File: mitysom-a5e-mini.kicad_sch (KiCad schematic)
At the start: 1 part, among them J1 Plug_Samtec_SEAM-50-02.0-L-08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

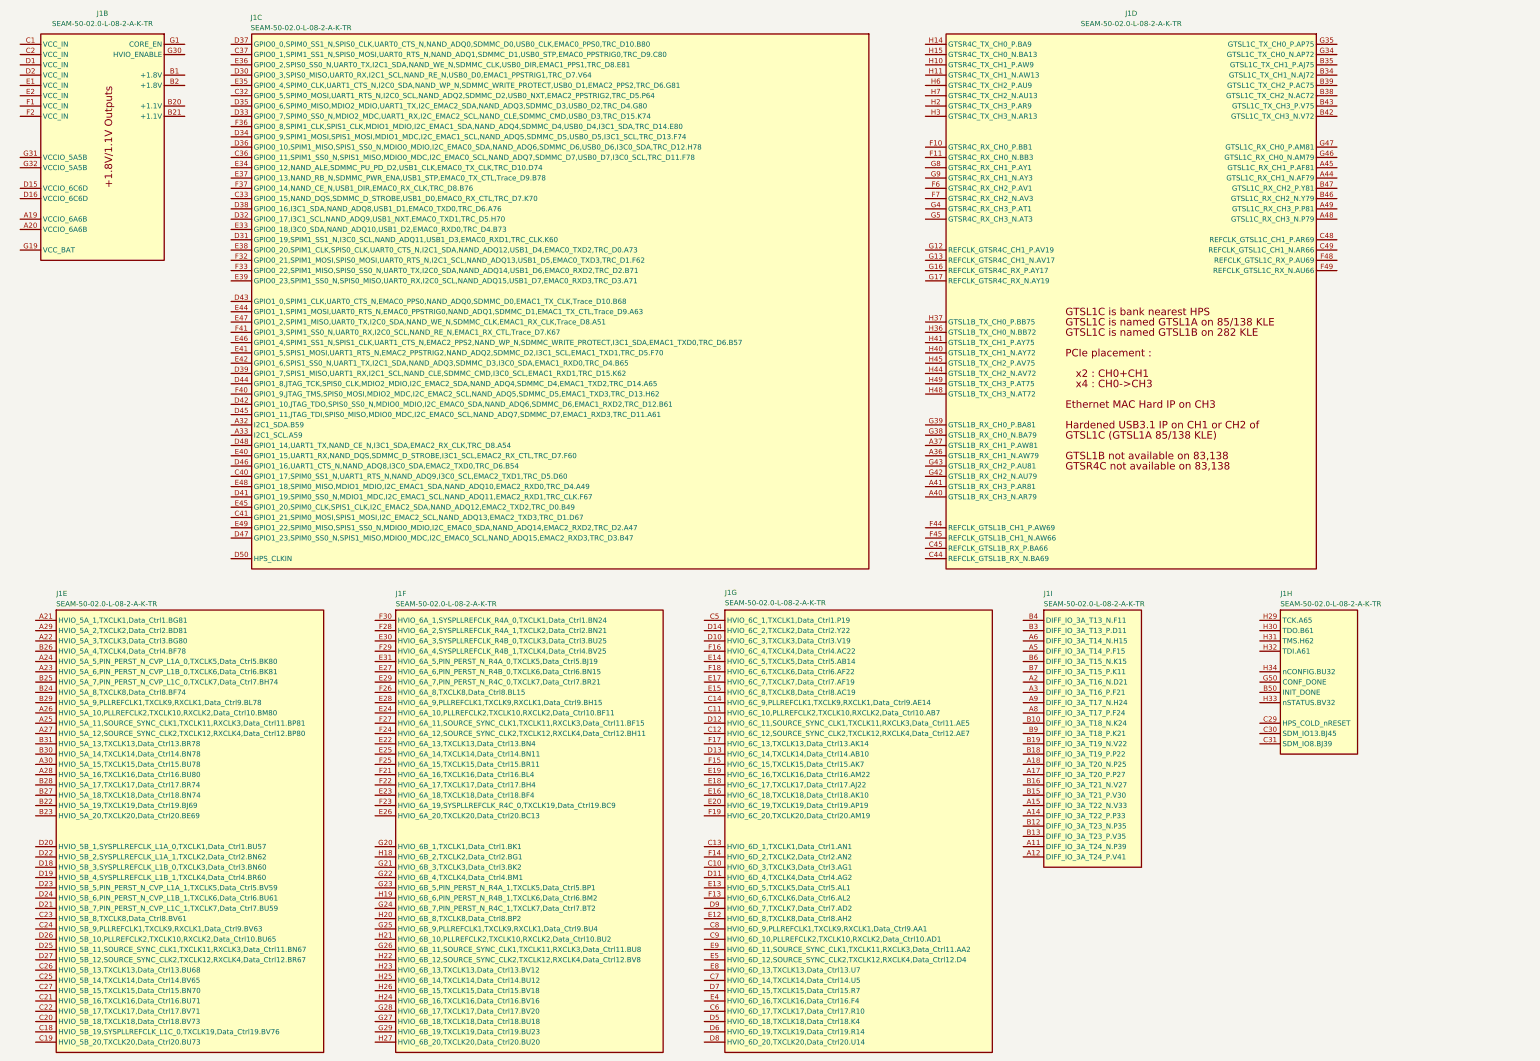
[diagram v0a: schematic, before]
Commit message: [#99649] Connect supply to MitySOM-A5E Mini
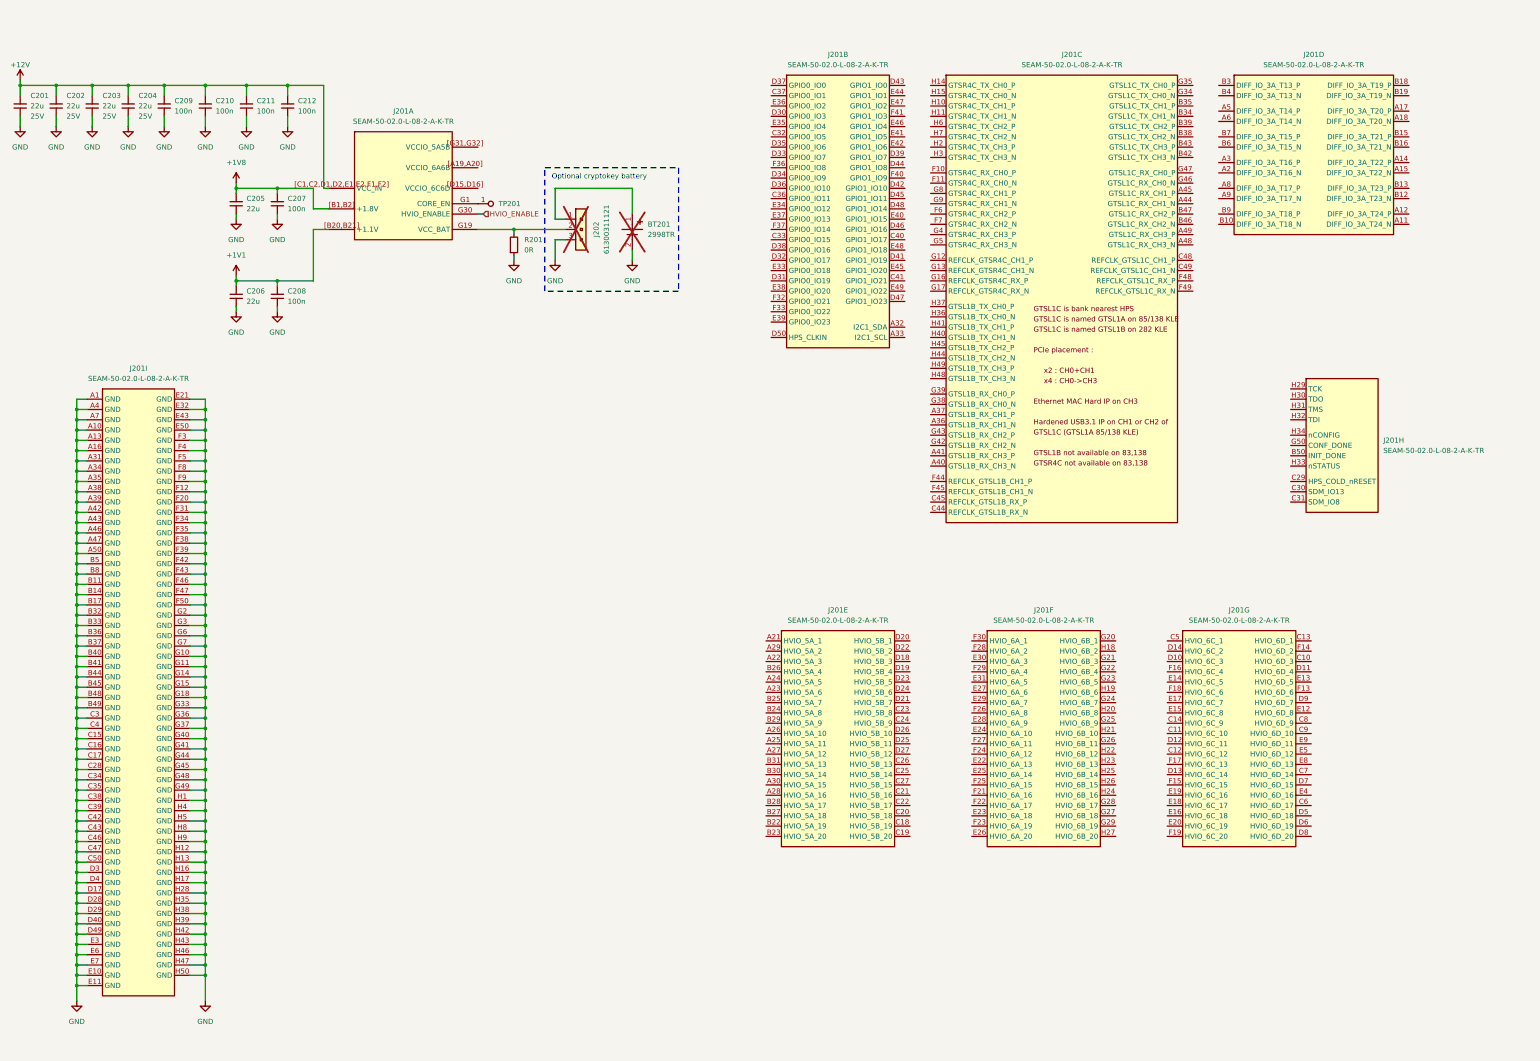
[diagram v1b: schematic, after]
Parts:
- removed J1: Plug_Samtec_SEAM-50-02.0-L-08-2-A-K-TR_CUSTOM_Mit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, antmicro-footprints:Conn_SEAM-50-02.0-L-08-2-A-K-TR, symbol antmicroB2BConnectors:Plug_Samtec_SEAM-50-02.0-L-08-2-A-K-TR_CUSTOM_MitySOM-A5E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
- added BT201: Battery_Holder_2998TR, antmicro-footprints:Battery_Holder_2998TR, symbol antmicroBatteryHoldersClipsContacts:Battery_Holder_2998TR
- added C201, C202, C203, C204: C_22u_25V_0805, antmicro-footprints:C_0805_2012Metric, symbol antmicroCapacitorsmisc:C_22u_25V_0805
- added C205, C206: C_22u_10V_0402, antmicro-footprints:C_0402_1005Metric, symbol antmicroCapacitors0402:C_22u_10V_0402
- added C207, C208, C209, C210, C211, C212: C_100n_0402, antmicro-footprints:C_0402_1005Metric, symbol antmicroCapacitors0402:C_100n_0402
- added J201: Plug_Samtec_SEAM-50-02.0-L-08-2-A-K-TR_CUSTOM_Mit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, antmicro-footprints:Conn_Plug_Samtec_SEAM-50-02.0-S-08-2-A-K-TR, symbol antmicroB2BConnectors:Plug_Samtec_SEAM-50-02.0-L-08-2-A-K-TR_CUSTOM_MitySOM-A5E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
- added J202: PinHeader_1x3_P2.54mm_Drill1.1mm, antmicro-footprints:PinHeader_1x3_P2.54mm_Drill1.1mm, symbol antmicroGenericPinHeaders:PinHeader_1x3_P2.54mm_Drill1.1mm
- added R201: R_0R_0402, antmicro-footprints:R_0402_1005Metric, symbol antmicroResistors0402:R_0R_0402
- added TP201: TP_1mm_SMD, antmicro-footprints:TP_SMD_1mm, symbol antmicroTestPoints:TP_1mm_SMD
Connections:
- new net: BT201.1 (V_BAT), J202.1
- new net: J201.G19 (VCC_BAT), J202.2, R201.2
- new net: J201.G1 (CORE_EN), TP201.1
- new net +12V: C201.2, C202.2, C203.2, C204.2, C209.2, C210.2, C211.2, C212.2, J201.[C1,C2,D1,D2,E1,E2,F1,F2] (VCC_IN)
- new net +1V1: C206.2, C208.2, J201.[B20,B21] (+1.1V)
- new net +1V8: C205.2, C207.2, J201.[B1,B2] (+1.8V)
- new net GND: BT201.2 (GND), C201.1, C202.1, C203.1, C204.1, C205.1, C206.1, C207.1, C208.1, C209.1, C210.1, C211.1, C212.1, J201.A1 (GND), J201.A10 (GND), J201.A13 (GND), J201.A16 (GND), J201.A31 (GND), J201.A34 (GND), J201.A35 (GND), J201.A38 (GND), J201.A39 (GND), J201.A4 (GND), J201.A42 (GND), J201.A43 (GND), J201.A46 (GND), J201.A47 (GND), J201.A50 (GND), J201.A7 (GND), J201.B11 (GND), J201.B14 (GND), J201.B17 (GND), J201.B32 (GND), J201.B33 (GND), J201.B36 (GND), J201.B37 (GND), J201.B40 (GND), J201.B41 (GND), J201.B44 (GND), J201.B45 (GND), J201.B48 (GND), J201.B49 (GND), J201.B5 (GND), J201.B8 (GND), J201.C15 (GND), J201.C16 (GND), J201.C17 (GND), J201.C28 (GND), J201.C3 (GND), J201.C34 (GND), J201.C35 (GND), J201.C38 (GND), J201.C39 (GND), J201.C4 (GND), J201.C42 (GND), J201.C43 (GND), J201.C46 (GND), J201.C47 (GND), J201.C50 (GND), J201.D17 (GND), J201.D28 (GND), J201.D29 (GND), J201.D3 (GND), J201.D4 (GND), J201.D40 (GND), J201.D49 (GND), J201.E10 (GND), J201.E11 (GND), J201.E21 (GND), J201.E3 (GND), J201.E32 (GND), J201.E43 (GND), J201.E50 (GND), J201.E6 (GND), J201.E7 (GND), J201.F12 (GND), J201.F20 (GND), J201.F3 (GND), J201.F31 (GND), J201.F34 (GND), J201.F35 (GND), J201.F38 (GND), J201.F39 (GND), J201.F4 (GND), J201.F42 (GND), J201.F43 (GND), J201.F46 (GND), J201.F47 (GND), J201.F5 (GND), J201.F50 (GND), J201.F8 (GND), J201.F9 (GND), J201.G10 (GND), J201.G11 (GND), J201.G14 (GND), J201.G15 (GND), J201.G18 (GND), J201.G2 (GND), J201.G3 (GND), J201.G33 (GND), J201.G36 (GND), J201.G37 (GND), J201.G40 (GND), J201.G41 (GND), J201.G44 (GND), J201.G45 (GND), J201.G48 (GND), J201.G49 (GND), J201.G6 (GND), J201.G7 (GND), J201.H1 (GND), J201.H12 (GND), J201.H13 (GND), J201.H16 (GND), J201.H17 (GND), J201.H28 (GND), J201.H35 (GND), J201.H38 (GND), J201.H39 (GND), J201.H4 (GND), J201.H42 (GND), J201.H43 (GND), J201.H46 (GND), J201.H47 (GND), J201.H5 (GND), J201.H50 (GND), J201.H8 (GND), J201.H9 (GND), J202.3, R201.1
- new net HVIO_ENABLE: J201.G30 (HVIO_ENABLE)
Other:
- note added: "Optional cryptokey battery"

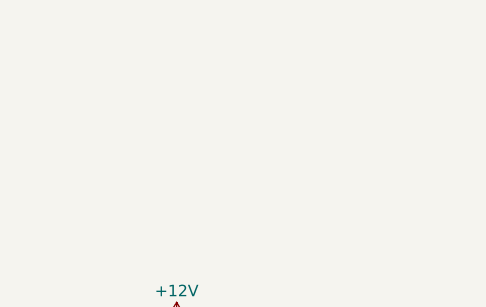
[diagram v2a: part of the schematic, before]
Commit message: [#99541] Add ULPI PHY schematic sheet
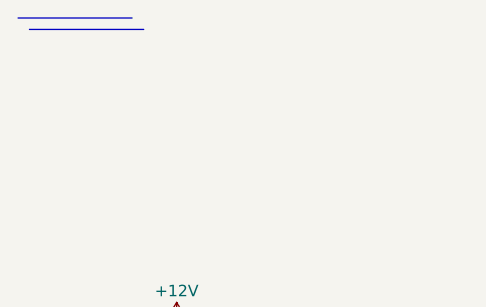
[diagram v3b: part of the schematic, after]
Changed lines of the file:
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@@
+		)
+	)
+	(bus
+		(pts
+			(xy 1.4224 1.4224) (xy 14.1224 1.4224)
+		)
+		(stroke
+			(width 0)
+			(type default)
 		)
 	)
@@
 		)
 		(stroke
+			(width 0)
+			(type default)
+		)
+	)
+	(bus
+		(pts
+			(xy 0.1524 0.1524) (xy 12.8524 0.1524)
+		)
+		(stroke

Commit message: [#99541] Connect ULPI, RGMII, SDIO and DisplayPort buses to MitySOM
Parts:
- added R202, R203, R204, R205, R206, R207: R_33R_0402, antmicro-footprints:R_0402_1005Metric, symbol antmicroResistors0402:R_33R_0402
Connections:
- net uSD.DAT2: now reaches J201.C32 (GPIO0_IO5)
- net ULPI.DATA0: now reaches J201.C33 (GPIO0_IO15)
- net uSD.DAT1: now reaches J201.C37 (GPIO0_IO1)
- net ULPI.DATA3: now reaches J201.D31 (GPIO0_IO19)
- net ULPI.NXT: now reaches J201.D32 (GPIO0_IO17)
- net uSD.CMD: now reaches J201.D33 (GPIO0_IO7)
- net uSD.DAT3: now reaches J201.D35 (GPIO0_IO6)
- net uSD.DAT0: now reaches J201.D37 (GPIO0_IO0)
- net ULPI.DATA1: now reaches J201.D38 (GPIO0_IO16)
- net GbE.RXD1: now reaches J201.D39 (GPIO1_IO7)
- net GbE.RXD2: now reaches J201.D42 (GPIO1_IO10)
- net GbE_TX_CLK: now reaches J201.D43 (GPIO1_IO0)
- net GbE_TX_CLK: now also R203.2
- net GbE_TXD2: now reaches J201.D44 (GPIO1_IO8)
- net GbE_TXD2: now also R207.2
- net GbE.RXD3: now reaches J201.D45 (GPIO1_IO11)
- net ULPI.DATA2: now reaches J201.E33 (GPIO0_IO18)
- net ULPI.CLK: now reaches J201.E34 (GPIO0_IO12)
- net uSD.~{CD}: now reaches J201.E35 (GPIO0_IO4)
- net uSD.CLK: now reaches J201.E36 (GPIO0_IO2)
- net ULPI.STP: now reaches J201.E37 (GPIO0_IO13)
- net ULPI.DATA4: now reaches J201.E38 (GPIO0_IO20)
- net ULPI.DATA7: now reaches J201.E39 (GPIO0_IO23)
- net GbE_TXD1: now reaches J201.E41 (GPIO1_IO5)
- net GbE_TXD1: now also R206.2
- net GbE.RXD0: now reaches J201.E42 (GPIO1_IO6)
- net GbE_TX_CTL: now reaches J201.E44 (GPIO1_IO1)
- net GbE_TX_CTL: now also R204.2
- net GbE_TXD0: now reaches J201.E46 (GPIO1_IO4)
- net GbE_TXD0: now also R205.2
- net GbE.RX_CLK: now reaches J201.E47 (GPIO1_IO2)
- net ULPI.DATA5: now reaches J201.F32 (GPIO0_IO21)
- net ULPI.DATA6: now reaches J201.F33 (GPIO0_IO22)
- net ULPI.DIR: now reaches J201.F37 (GPIO0_IO14)
- net GbE_TXD3: now reaches J201.F40 (GPIO1_IO9)
- net GbE_TXD3: now also R202.2
- net GbE.RX_CTL: now reaches J201.F41 (GPIO1_IO3)
- net DP.TXD0-: now reaches J201.H36 (GTSL1B_TX_CH0_N)
- net DP.TXD0+: now reaches J201.H37 (GTSL1B_TX_CH0_P)
- net DP.TXD1-: now reaches J201.H40 (GTSL1B_TX_CH1_N)
- net DP.TXD1+: now reaches J201.H41 (GTSL1B_TX_CH1_P)
- net DP.TXD2-: now reaches J201.H44 (GTSL1B_TX_CH2_N)
- net DP.TXD2+: now reaches J201.H45 (GTSL1B_TX_CH2_P)
- net DP.TXD3-: now reaches J201.H48 (GTSL1B_TX_CH3_N)
- net DP.TXD3+: now reaches J201.H49 (GTSL1B_TX_CH3_P)
- new net GbE.TXD0: R205.1
- new net GbE.TXD1: R206.1
- new net GbE.TXD2: R207.1
- new net GbE.TXD3: R202.1
- new net GbE.TX_CLK: R203.1
- new net GbE.TX_CTL: R204.1
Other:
- moved on the sheet: J201B, J201C, J201D, J201E, J201F, J201G, J201H

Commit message: [#99541] Connect MDIO, JTAG to MitySOM
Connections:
- net ULPI.~{RST}: now reaches J201.D30 (GPIO0_IO3)
- net GbE.MDC: now reaches J201.D41 (GPIO1_IO19)
- net GbE.MDIO: now reaches J201.E48 (GPIO1_IO18)
- net SDM.TCK: now reaches J201.H29 (TCK)
- net SDM.TDO: now reaches J201.H30 (TDO)
- net SDM.TMS: now reaches J201.H31 (TMS)
- net SDM.TDI: now reaches J201.H32 (TDI)
- net ULPI.DATA0 renamed ULPI.DAT0
- net ULPI.DATA1 renamed ULPI.DAT1
- net ULPI.DATA2 renamed ULPI.DAT2
- net ULPI.DATA3 renamed ULPI.DAT3
- net ULPI.DATA4 renamed ULPI.DAT4
- net ULPI.DATA5 renamed ULPI.DAT5
- net ULPI.DATA6 renamed ULPI.DAT6
- net ULPI.DATA7 renamed ULPI.DAT7
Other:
- moved on the sheet: J201C, J201H
